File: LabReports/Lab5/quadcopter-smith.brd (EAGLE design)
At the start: 95.4 x 95.4 mm, 58 parts, among them J1 AVR_SPI_PRG_6NS, Q1 SI2302CDS, Q2 SI2302CDS, Q3 SI2302CDS, Q4 SI2302CDS, U1 ATMEGA128RFA1, U2 LSM9DS0-LGA24, Y1 16MHz

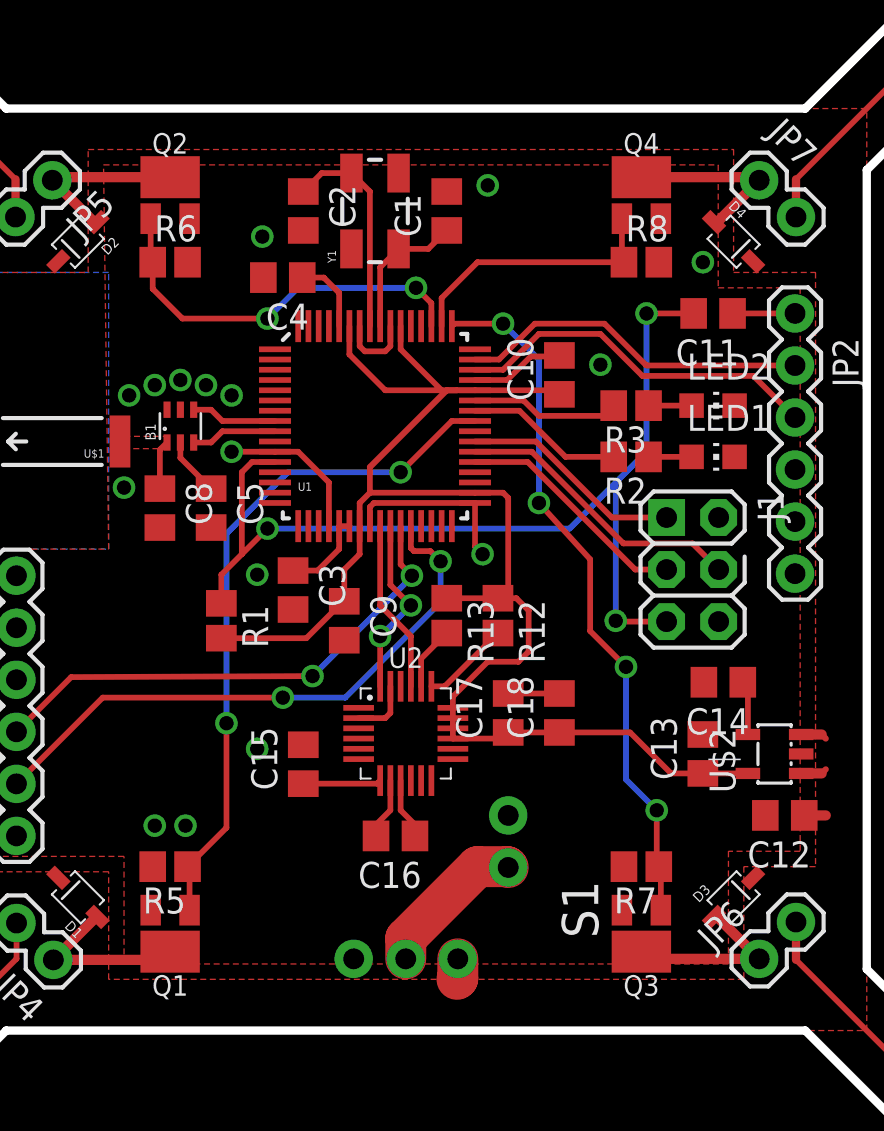
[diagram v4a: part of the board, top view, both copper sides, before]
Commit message: Tweaked gnd via placement
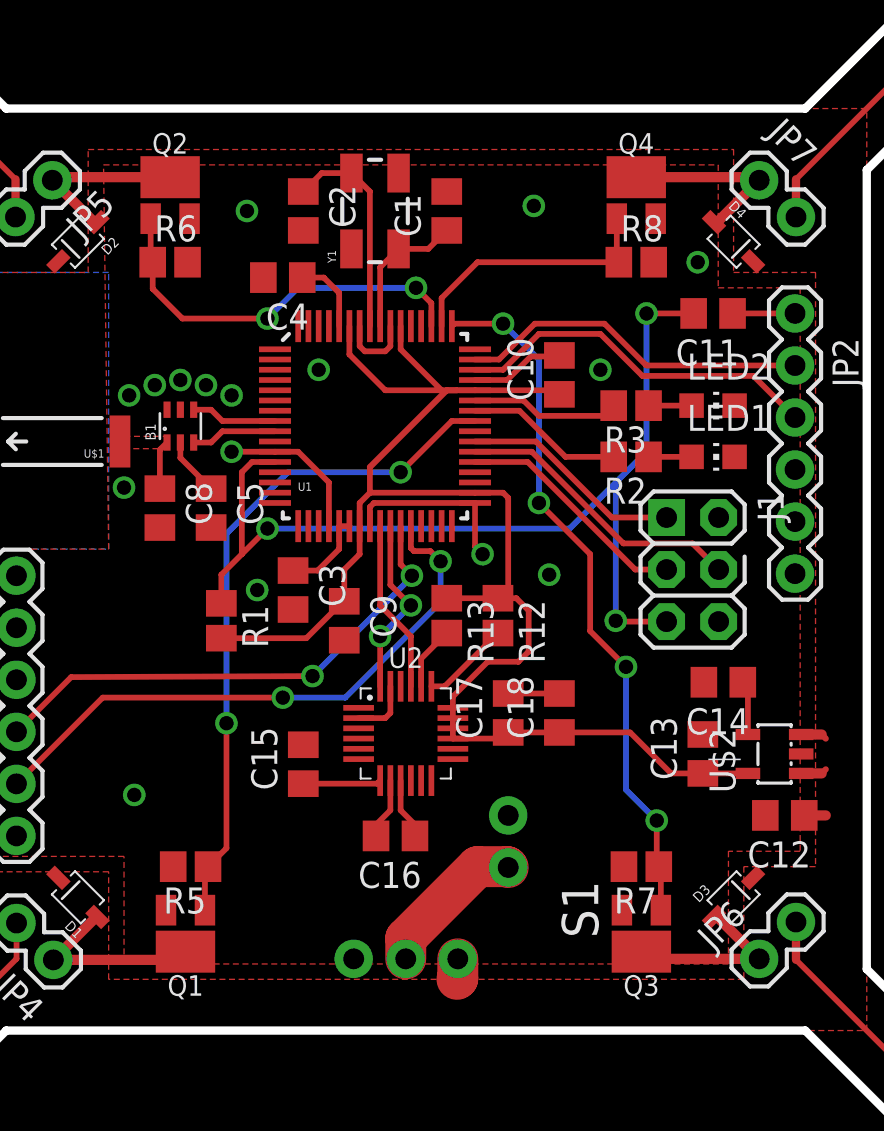
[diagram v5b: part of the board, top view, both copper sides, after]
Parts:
- moved R5 1.00 mm to (-10.5, -14.5)
- moved Q1 0.75 mm to (-10.8, -17.5)
- moved Q4 0.25 mm to (11.2, 18.0)
- moved R8 0.25 mm to (11.2, 15.0)
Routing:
- net N$18: track 8.89 -> 9.54 mm
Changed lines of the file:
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@@
 <element name="LED6" library="Lab5" package="CHIP-LED0805" value="GREEN" x="32.5" y="32.5" rot="R315"/>
 <element name="LED7" library="Lab5" package="CHIP-LED0805" value="RED" x="32.5" y="-32.5" rot="R225"/>
-<element name="Q1" library="Trevor-lab4" package="SOT-23" value="SI2302CDS" x="-11.5" y="-17.5" rot="R180">
-<attribute name="CREATOR" value="Trevor Smith" x="-11.5" y="-17.5" size="1.778" layer="27" rot="R180" display="off"/>
-<attribute name="DISTPN" value="SI2302CDS-T1-E3" x="-11.5" y="-17.5" size="1.778" layer="27" rot="R180" display="off"/>
-<attribute name="DIST" value="Digikey" x="-11.5" y="-17.5" size="1.778" layer="27" rot="R180" display="off"/>
+<element name="Q1" library="Trevor-lab4" package="SOT-23" value="SI2302CDS" x="-10.75" y="-17.5" rot="R180">
+<attribute name="CREATOR" value="Trevor Smith" x="-10.75" y="-17.5" size="1.778" layer="27" rot="R180" display="off"/>
+<attribute name="DISTPN" value="SI2302CDS-T1-E3" x="-10.75" y="-17.5" size="1.778" layer="27" rot="R180" display="off"/>
+<attribute name="DIST" value="Digikey" x="-10.75" y="-17.5" size="1.778" layer="27" rot="R180" display="off"/>
 </element>
 <element name="Q2" library="Trevor-lab4" package="SOT-23" value="SI2302CDS" x="-11.5" y="18">
@@
 <attribute name="DIST" value="Digikey" x="11.5" y="-17.5" size="1.778" layer="27" rot="R180" display="off"/>
 </element>
-<element name="Q4" library="Trevor-lab4" package="SOT-23" value="SI2302CDS" x="11.5" y="18">
-<attribute name="CREATOR" value="Trevor Smith" x="11.5" y="18" size="1.778" layer="27" display="off"/>
-<attribute name="DISTPN" value="SI2302CDS-T1-E3" x="11.5" y="18" size="1.778" layer="27" display="off"/>
-<attribute name="DIST" value="Digikey" x="11.5" y="18" size="1.778" layer="27" display="off"/>
+<element name="Q4" library="Trevor-lab4" package="SOT-23" value="SI2302CDS" x="11.25" y="18">
+<attribute name="CREATOR" value="Trevor Smith" x="11.25" y="18" size="1.778" layer="27" display="off"/>
+<attribute name="DISTPN" value="SI2302CDS-T1-E3" x="11.25" y="18" size="1.778" layer="27" display="off"/>
+<attribute name="DIST" value="Digikey" x="11.25" y="18" size="1.778" layer="27" display="off"/>
 </element>
 <element name="R1" library="Lab5" package="R0805" value="10k" x="-9" y="-2.5" rot="R270"/>
@@
 <element name="R3" library="Lab5" package="R0805" value="270" x="11" y="8" rot="R180"/>
 <element name="R4" library="Lab5" package="R0805" value="30" x="-26.5" y="26.5" rot="R315"/>
-<element name="R5" library="Lab5" package="R0805" value="10k" x="-11.5" y="-14.5" rot="R180"/>
+<element name="R5" library="Lab5" package="R0805" value="10k" x="-10.5" y="-14.5" rot="R180"/>
 <element name="R6" library="Lab5" package="R0805" value="10k" x="-11.5" y="15"/>
 <element name="R7" library="Lab5" package="R0805" value="10k" x="11.5" y="-14.5" rot="R180"/>
-<element name="R8" library="Lab5" package="R0805" value="10k" x="11.5" y="15"/>
+<element name="R8" library="Lab5" package="R0805" value="10k" x="11.25" y="15"/>
 <element name="R9" library="Lab5" package="R0805" value="100" x="-26.5" y="-26.5" rot="R45"/>
 <element name="S1" library="Lab5" package="SWITCH-SPDT" value="" x="0" y="-19" rot="R270">
@@
 <wire x1="7.45" y1="10.4" x2="6.1" y2="10.4" width="0.28" layer="1"/>
 <wire x1="5" y1="-6.05" x2="7.5" y2="-6.05" width="0.28" layer="1"/>
-<via x="9.5" y="10" extent="1-16" drill="0.7"/>
+<via x="9.5" y="9.75" extent="1-16" drill="0.7"/>
 <wire x1="-0.75" y1="-5.7" x2="-0.75" y2="-7" width="0.28" layer="1"/>
 <wire x1="-0.75" y1="-7" x2="-1" y2="-7.25" width="0.28" layer="1"/>
@@
 <vertex x="-36" y="14.5"/>
 </polygon>
-<via x="14.5" y="15" extent="1-16" drill="0.7"/>
-<via x="-7.25" y="-0.25" extent="1-16" drill="0.7"/>
+<via x="-7.25" y="-1" extent="1-16" drill="0.7"/>
 <via x="3.75" y="0.75" extent="1-16" drill="0.7"/>
 <wire x1="3.381" y1="3.25" x2="3.381" y2="1.119" width="0.28" layer="1"/>
@@
 <wire x1="-1" y1="10.65" x2="-0.75" y2="10.9" width="0.28" layer="1"/>
 <wire x1="-0.75" y1="10.9" x2="-0.75" y2="11.881" width="0.28" layer="1"/>
-<via x="-7" y="16.25" extent="1-16" drill="0.7"/>
-<via x="4" y="18.75" extent="1-16" drill="0.7"/>
-<via x="-7.25" y="-8.75" extent="1-16" drill="0.7"/>
-<via x="-12.25" y="-12.5" extent="1-16" drill="0.7"/>
-<via x="-10.75" y="-12.5" extent="1-16" drill="0.7"/>
+<via x="-7.75" y="17.5" extent="1-16" drill="0.7"/>
+<via x="6.25" y="17.75" extent="1-16" drill="0.7"/>
+<via x="-13.25" y="-11" extent="1-16" drill="0.7"/>
 <polygon width="0.3" layer="1" rank="2">
 <vertex x="-14.75" y="19.75"/>
@@
 <vertex x="-14.5" y="1"/>
 </polygon>
+<via x="14.25" y="15" extent="1-16" drill="0.7"/>
+<via x="-4.25" y="9.75" extent="1-16" drill="0.7"/>
+<via x="7" y="-0.25" extent="1-16" drill="0.7"/>
 </signal>
 <signal name="N$3">
@@
 <contactref element="R5" pad="1"/>
 <contactref element="Q1" pad="P$1"/>
-<wire x1="-10.55" y1="-16.625" x2="-10.55" y2="-14.6" width="0.28" layer="1"/>
-<wire x1="-10.55" y1="-14.6" x2="-10.65" y2="-14.5" width="0.28" layer="1"/>
+<wire x1="-9.8" y1="-16.625" x2="-9.8" y2="-14.85" width="0.28" layer="1"/>
+<wire x1="-9.8" y1="-14.85" x2="-9.65" y2="-14.5" width="0.28" layer="1"/>
 <wire x1="3.381" y1="7.25" x2="2.25" y2="7.25" width="0.28" layer="1"/>
 <wire x1="2.25" y1="7.25" x2="-0.25" y2="4.75" width="0.28" layer="1"/>
@@
 <wire x1="-8.75" y1="1.75" x2="-8.75" y2="-7.5" width="0.28" layer="16"/>
 <via x="-8.75" y="-7.5" extent="1-16" drill="0.7"/>
-<wire x1="-8.75" y1="-7.5" x2="-8.75" y2="-12.6" width="0.28" layer="1"/>
-<wire x1="-8.75" y1="-12.6" x2="-10.65" y2="-14.5" width="0.28" layer="1"/>
+<wire x1="-8.75" y1="-7.5" x2="-8.75" y2="-13.6" width="0.28" layer="1"/>
+<wire x1="-8.75" y1="-13.6" x2="-9.65" y2="-14.5" width="0.28" layer="1"/>
 </signal>
 <signal name="PB6">
@@
 <wire x1="6.5" y1="10.25" x2="6.5" y2="3.25" width="0.28" layer="16"/>
 <via x="6.5" y="3.25" extent="1-16" drill="0.7"/>
-<wire x1="6.5" y1="3.25" x2="9" y2="0.5" width="0.28" layer="1"/>
-<wire x1="9" y1="0.5" x2="9" y2="-3" width="0.28" layer="1"/>
+<wire x1="6.5" y1="3.25" x2="9" y2="0.75" width="0.28" layer="1"/>
+<wire x1="9" y1="0.75" x2="9" y2="-3" width="0.28" layer="1"/>
 <wire x1="9" y1="-3" x2="10.75" y2="-4.75" width="0.28" layer="1"/>
 <via x="10.75" y="-4.75" extent="1-16" drill="0.7"/>
-<wire x1="10.75" y1="-4.75" x2="10.75" y2="-10.25" width="0.28" layer="16"/>
-<wire x1="10.75" y1="-10.25" x2="12.25" y2="-11.75" width="0.28" layer="16"/>
-<via x="12.25" y="-11.75" extent="1-16" drill="0.7"/>
-<wire x1="12.25" y1="-11.75" x2="12.25" y2="-14.4" width="0.28" layer="1"/>
+<wire x1="10.75" y1="-4.75" x2="10.75" y2="-10.75" width="0.28" layer="16"/>
+<wire x1="10.75" y1="-10.75" x2="12.25" y2="-12.25" width="0.28" layer="16"/>
+<via x="12.25" y="-12.25" extent="1-16" drill="0.7"/>
+<wire x1="12.25" y1="-12.25" x2="12.25" y2="-14.4" width="0.28" layer="1"/>
 <wire x1="12.25" y1="-14.4" x2="12.35" y2="-14.5" width="0.28" layer="1"/>
 <wire x1="4.75" y1="12" x2="2.369" y2="12" width="0.28" layer="1"/>
@@
 <wire x1="1.75" y1="11.881" x2="1.75" y2="13.25" width="0.28" layer="1"/>
 <wire x1="1.75" y1="13.25" x2="3.5" y2="15" width="0.28" layer="1"/>
-<wire x1="3.5" y1="15" x2="10.65" y2="15" width="0.28" layer="1"/>
-<wire x1="10.55" y1="17.125" x2="10.55" y2="15.1" width="0.28" layer="1"/>
-<wire x1="10.55" y1="15.1" x2="10.65" y2="15" width="0.28" layer="1"/>
+<wire x1="3.5" y1="15" x2="10.4" y2="15" width="0.28" layer="1"/>
+<wire x1="10.3" y1="17.125" x2="10.3" y2="15.1" width="0.28" layer="1"/>
+<wire x1="10.3" y1="15.1" x2="10.4" y2="15" width="0.28" layer="1"/>
 </signal>
 <signal name="PE7">
@@
 <wire x1="-17.2" y1="-19.05" x2="-15.10459375" y2="-16.95459375" width="0.5" layer="1"/>
 <wire x1="-15.10459375" y1="-16.95459375" x2="-15.045403125" y2="-16.95459375" width="0.5" layer="1"/>
-<wire x1="-11.5" y1="-18.65" x2="-11.9" y2="-19.05" width="0.5" layer="1"/>
+<wire x1="-10.75" y1="-18.65" x2="-11.9" y2="-19.05" width="0.5" layer="1"/>
 <wire x1="-11.9" y1="-19.05" x2="-17.2" y2="-19.05" width="0.5" layer="1"/>
 </signal>
@@
 <wire x1="15.045403125" y1="16.95459375" x2="15.20459375" y2="16.95459375" width="0.5" layer="1"/>
 <wire x1="15.20459375" y1="16.95459375" x2="17.25" y2="19" width="0.5" layer="1"/>
-<wire x1="11.5" y1="19.15" x2="17.1" y2="19.15" width="0.5" layer="1"/>
+<wire x1="11.25" y1="19.15" x2="17.1" y2="19.15" width="0.5" layer="1"/>
 <wire x1="17.1" y1="19.15" x2="17.25" y2="19" width="0.5" layer="1"/>
 </signal>

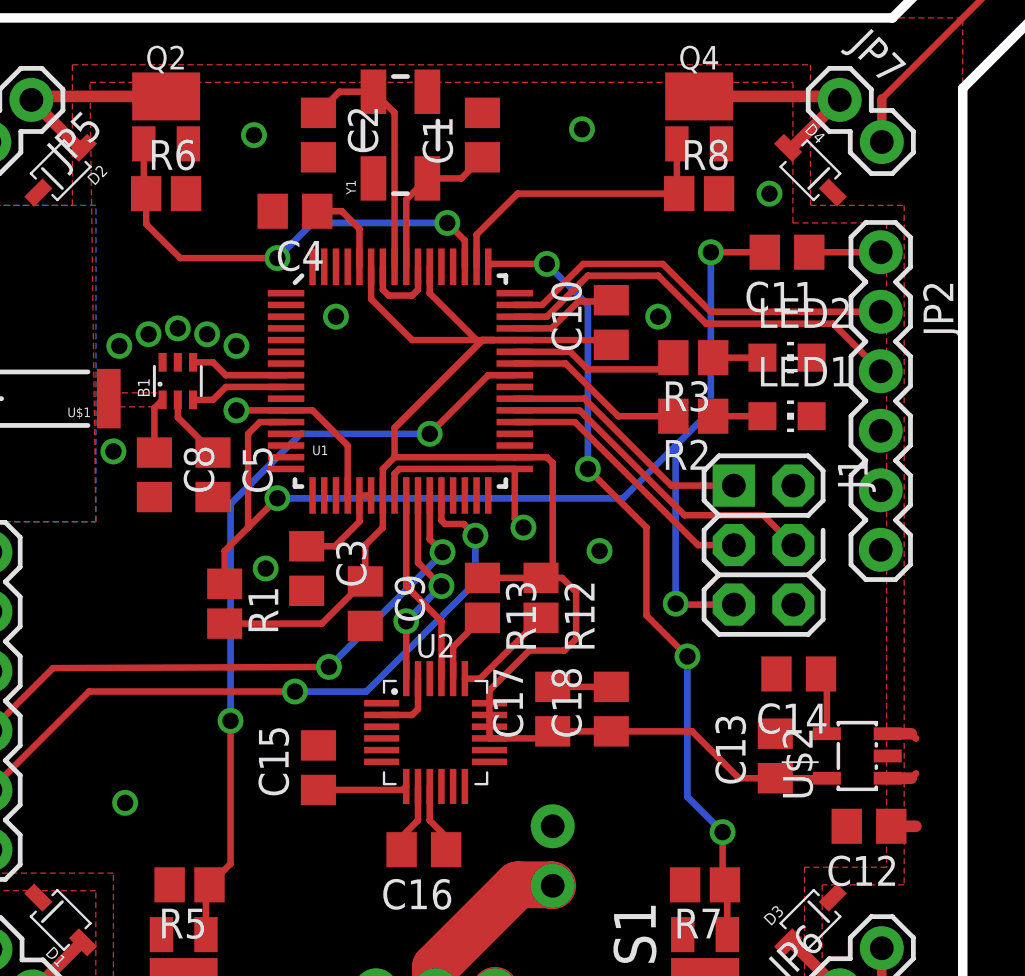
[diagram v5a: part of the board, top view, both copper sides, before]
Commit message: Adjusted some ground paths
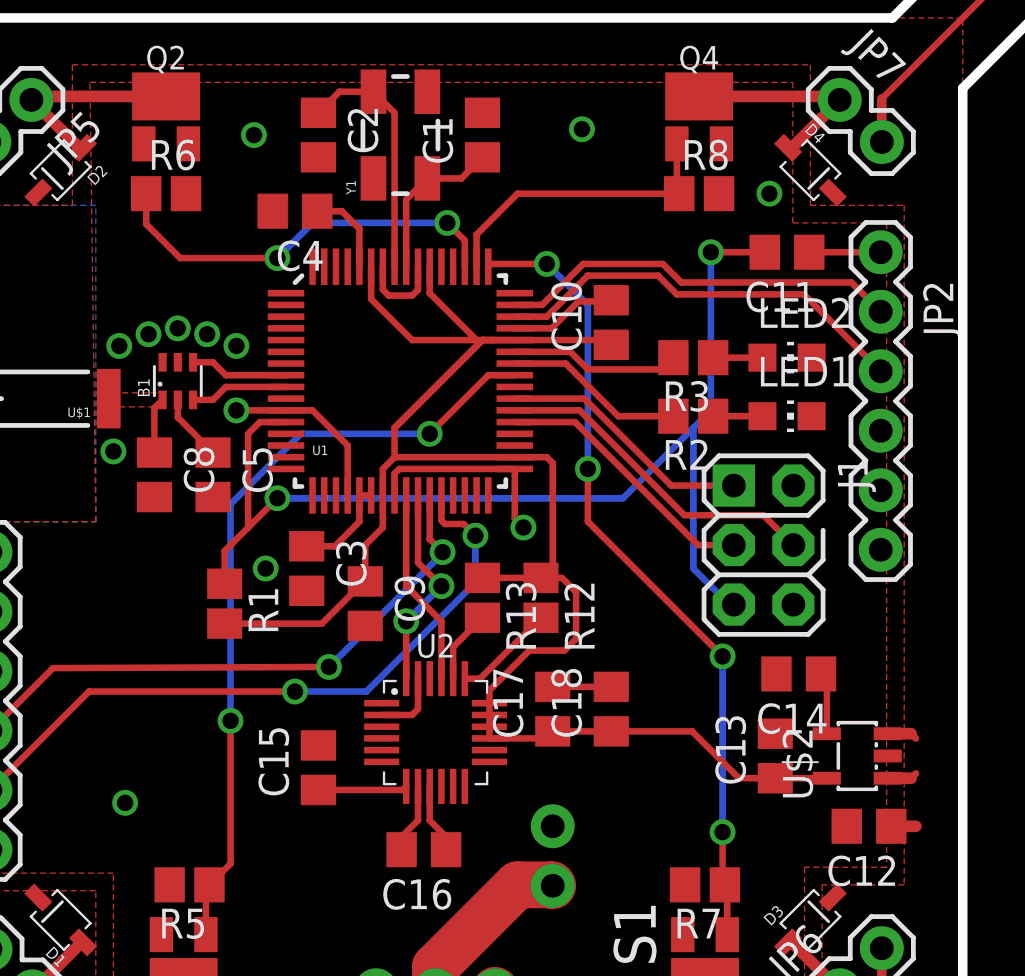
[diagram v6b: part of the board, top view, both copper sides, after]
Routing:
- net PE5: track 19.7 -> 17.7 mm
- net RESET: track 48.8 -> 47.9 mm, vias 3 -> 2
- net GND: vias 20 -> 17
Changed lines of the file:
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@@
 <wire x1="7.45" y1="10.4" x2="6.1" y2="10.4" width="0.28" layer="1"/>
 <wire x1="5" y1="-6.05" x2="7.5" y2="-6.05" width="0.28" layer="1"/>
-<via x="9.5" y="9.75" extent="1-16" drill="0.7"/>
 <wire x1="-0.75" y1="-5.7" x2="-0.75" y2="-7" width="0.28" layer="1"/>
 <wire x1="-0.75" y1="-7" x2="-1" y2="-7.25" width="0.28" layer="1"/>
@@
 </polygon>
 <via x="14.25" y="15" extent="1-16" drill="0.7"/>
-<via x="-4.25" y="9.75" extent="1-16" drill="0.7"/>
-<via x="7" y="-0.25" extent="1-16" drill="0.7"/>
 </signal>
 <signal name="N$3">
@@
 <wire x1="4.75" y1="9.75" x2="6.5" y2="11.5" width="0.28" layer="1"/>
 <wire x1="6.5" y1="11.5" x2="9.5" y2="11.5" width="0.28" layer="1"/>
-<wire x1="9.5" y1="11.5" x2="11.55" y2="9.45" width="0.28" layer="1"/>
-<wire x1="11.55" y1="9.45" x2="16.97" y2="9.45" width="0.28" layer="1"/>
-<wire x1="16.97" y1="9.45" x2="19" y2="7.42" width="0.28" layer="1"/>
+<wire x1="9.5" y1="11.5" x2="10.3" y2="10.7" width="0.28" layer="1"/>
+<wire x1="10.3" y1="10.7" x2="15.72" y2="10.7" width="0.28" layer="1"/>
+<wire x1="15.72" y1="10.7" x2="19" y2="7.42" width="0.28" layer="1"/>
 </signal>
 <signal name="PE2">
@@
 <wire x1="6.5" y1="10.25" x2="6.5" y2="3.25" width="0.28" layer="16"/>
 <via x="6.5" y="3.25" extent="1-16" drill="0.7"/>
-<wire x1="6.5" y1="3.25" x2="9" y2="0.75" width="0.28" layer="1"/>
-<wire x1="9" y1="0.75" x2="9" y2="-3" width="0.28" layer="1"/>
-<wire x1="9" y1="-3" x2="10.75" y2="-4.75" width="0.28" layer="1"/>
-<via x="10.75" y="-4.75" extent="1-16" drill="0.7"/>
-<wire x1="10.75" y1="-4.75" x2="10.75" y2="-10.75" width="0.28" layer="16"/>
-<wire x1="10.75" y1="-10.75" x2="12.25" y2="-12.25" width="0.28" layer="16"/>
+<wire x1="6.5" y1="3.25" x2="6.5" y2="1" width="0.28" layer="1"/>
+<wire x1="6.5" y1="1" x2="12.25" y2="-4.75" width="0.28" layer="1"/>
+<via x="12.25" y="-4.75" extent="1-16" drill="0.7"/>
+<wire x1="12.25" y1="-4.75" x2="12.25" y2="-12.25" width="0.28" layer="16"/>
 <via x="12.25" y="-12.25" extent="1-16" drill="0.7"/>
 <wire x1="12.25" y1="-12.25" x2="12.25" y2="-14.4" width="0.28" layer="1"/>
@@
 <contactref element="R6" pad="1"/>
 <contactref element="Q2" pad="P$1"/>
-<wire x1="-12.45" y1="17.125" x2="-12.45" y2="15.1" width="0.28" layer="1"/>
 <wire x1="-12.45" y1="15.1" x2="-12.35" y2="15" width="0.28" layer="1"/>
 <wire x1="1.25" y1="11.881" x2="1.25" y2="13" width="0.28" layer="1"/>
@@
 <wire x1="-10.9" y1="12.25" x2="-12.35" y2="13.7" width="0.28" layer="1"/>
 <wire x1="-12.35" y1="15" x2="-12.35" y2="13.7" width="0.28" layer="1"/>
+<wire x1="-12.45" y1="15.1" x2="-12.45" y2="17.125" width="0" layer="19" extent="1-1"/>
 </signal>
 <signal name="PE6">
@@
 <wire x1="4.55" y1="10.25" x2="6.3" y2="12" width="0.28" layer="1"/>
 <wire x1="6.3" y1="12" x2="9.7" y2="12" width="0.28" layer="1"/>
-<wire x1="9.7" y1="12" x2="11.74" y2="9.96" width="0.28" layer="1"/>
-<wire x1="11.74" y1="9.96" x2="19" y2="9.96" width="0.28" layer="1"/>
+<wire x1="9.7" y1="12" x2="10.49" y2="11.21" width="0.28" layer="1"/>
+<wire x1="10.49" y1="11.21" x2="17.75" y2="11.21" width="0.28" layer="1"/>
+<wire x1="17.75" y1="11.21" x2="19" y2="9.96" width="0.28" layer="1"/>
 </signal>
 <signal name="N$12">
@@
 <via x="11.75" y="12.5" extent="1-16" drill="0.7"/>
 <wire x1="11.75" y1="12.5" x2="11.75" y2="5.75" width="0.28" layer="16"/>
-<wire x1="11.75" y1="5.75" x2="10.25" y2="4.25" width="0.28" layer="16"/>
-<wire x1="10.25" y1="4.25" x2="10.25" y2="-2.5" width="0.28" layer="16"/>
-<via x="10.25" y="-2.5" extent="1-16" drill="0.7"/>
-<wire x1="10.25" y1="-2.5" x2="10.29" y2="-2.54" width="0.28" layer="1"/>
-<wire x1="10.29" y1="-2.54" x2="12.73" y2="-2.54" width="0.28" layer="1"/>
-<wire x1="10.25" y1="4.25" x2="8" y2="2" width="0.28" layer="16"/>
+<wire x1="11.75" y1="5.75" x2="11" y2="5" width="0.28" layer="16"/>
+<wire x1="11" y1="5" x2="11" y2="-1" width="0.28" layer="16"/>
+<wire x1="11" y1="5" x2="8" y2="2" width="0.28" layer="16"/>
 <wire x1="8" y1="2" x2="-6.75" y2="2" width="0.28" layer="16"/>
 <via x="-6.75" y="2" extent="1-16" drill="0.7"/>
 <wire x1="-6.75" y1="2" x2="-8" y2="0.75" width="0.28" layer="1"/>
 <wire x1="-8" y1="0.75" x2="-9" y2="-0.25" width="0.28" layer="1"/>
+<wire x1="12.73" y1="-2.54" x2="12.54" y2="-2.54" width="0.28" layer="16"/>
+<wire x1="12.54" y1="-2.54" x2="11" y2="-1" width="0.28" layer="16"/>
 </signal>
 <signal name="N$18">

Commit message: prepared board for peer review, exported CAM files
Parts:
- moved Q3 0.50 mm to (11.5, -17.0)
- moved R7 0.50 mm to (11.5, -14.0)
- moved D3 0.25 mm to (16.0, -15.8)
- moved JP6 0.25 mm to (17.2, -18.8)
- flipped JP1 to the top
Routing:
- net PE5: track 17.7 -> 19.7 mm
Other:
- board text added: "DEBUGGER"
- board text added: "GND"
- board text added: "X"
- board text added: "Y"
